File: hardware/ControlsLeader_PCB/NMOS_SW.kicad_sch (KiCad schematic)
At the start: 4 parts, among them Q15 NMOS

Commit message: DONE!!! - just need to add footprints + part #s)
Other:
- note added: "NMOS 24v -> 3.3v Signal Converter"
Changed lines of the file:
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@@
+		)
+	)
+	(text "NMOS 24v -> 3.3v Signal Converter"
+		(exclude_from_sim no)
+		(at 141.478 70.104 0)
+		(effects
+			(font
+				(size 1.905 1.905)
+				(thickness 0.254)
+				(bold yes)
+			)
 		)
 	)

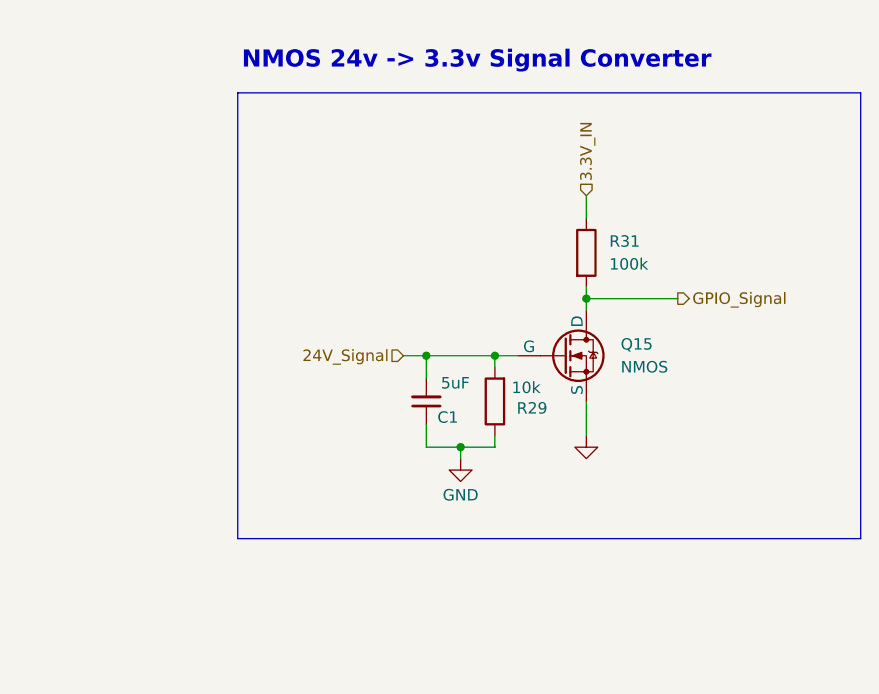
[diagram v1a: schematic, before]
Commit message: Schematic Ready for Review - Just need FET footprints to be confirmed
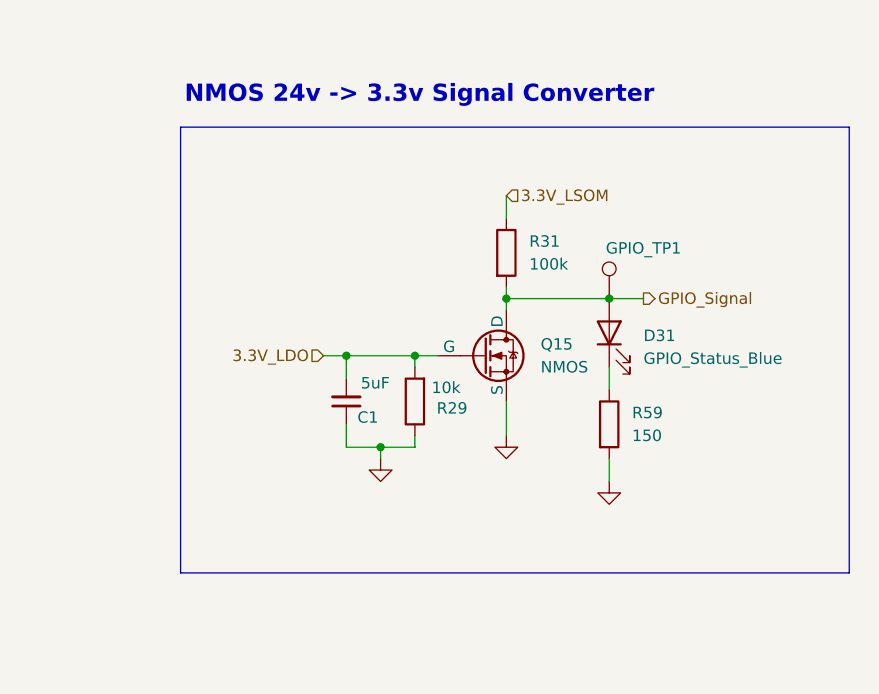
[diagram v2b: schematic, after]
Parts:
- added D31: GPIO_Status_Blue, LED_SMD:LED_0201_0603Metric_Pad0.64x0.40mm_HandSolder, symbol Device:LED
- added GPIO_TP1: TestPoint, TestPoint:TestPoint_Pad_1.0x1.0mm, symbol Connector:TestPoint
- added R59: 150, Capacitor_SMD:C_0201_0603Metric_Pad0.64x0.40mm_HandSolder, symbol Device:R
- C1: footprint Capacitor_SMD:C_0805_2012Metric -> Capacitor_SMD:C_0603_1608Metric_Pad1.08x0.95mm_HandSolder
- R29: footprint Resistor_SMD:R_0805_2012Metric -> Capacitor_SMD:C_0201_0603Metric_Pad0.64x0.40mm_HandSolder
- R31: footprint (none) -> Capacitor_SMD:C_0201_0603Metric_Pad0.64x0.40mm_HandSolder
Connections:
- net GND: now also R59.2
- net GPIO_Signal: now also D31.2 (A), GPIO_TP1.1
- net 24V_Signal renamed 3.3V_LDO
- net 3.3V_IN renamed 3.3V_LSOM
- new net: D31.1 (K), R59.1
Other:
- moved on the sheet: C1, Q15, R29, R31

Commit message: Ready for final review
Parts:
- D1: renamed from D31; Distributor Link (none) -> https://www.digikey.com/en/products/detail/ams-osram-usa-in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; Manufacturer (none) -> DigiKey; Manufacturer Prt # (none) -> LB Q99G.01-P1R1-35-1-5-R18
- Q15: footprint (none) -> LSOM_IRLM:SOT23
- renumbered R29 to R16, R31 to R17, R59 to R29, GPIO_TP1 to TP2
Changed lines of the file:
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@@
 		(dnp no)
 		(fields_autoplaced yes)
-		(property "Reference" "#PWR049"
+		(property "Reference" "#PWR036"
 			(at 156.21 123.19 0)
 			(effects
@@
 		(instances
 			(project "ControlsLeader_PCB"
-				(path "/298dad81-302c-41c7-874b-fcde1c3cde17/b17bad26-1d2e-4521-b2ad-37a0683696f4"
-					(reference "#PWR049")
-					(unit 1)
-				)
 				(path "/298dad81-302c-41c7-874b-fcde1c3cde17/cf34858a-7a31-4837-b51d-ee9ae3dd074c/879fa84f-14ed-4d21-9f88-1baa6fbdbf33"
 					(reference "#PWR087")
@@
 				(path "/298dad81-302c-41c7-874b-fcde1c3cde17/cf34858a-7a31-4837-b51d-ee9ae3dd074c/ed43737a-66c9-4099-9c79-193ec40f0132"
 					(reference "#PWR088")
+					(unit 1)
+				)
+				(path "/298dad81-302c-41c7-874b-fcde1c3cde17/cf34858a-7a31-4837-b51d-ee9ae3dd074c/f6cf8ad6-a024-4eda-a711-34d588471472"
+					(reference "#PWR036")
 					(unit 1)
 				)
@@
 		(dnp no)
 		(fields_autoplaced yes)
-		(property "Reference" "#PWR072"
+		(property "Reference" "#PWR033"
 			(at 144.78 118.11 0)
 			(effects
@@
 		(instances
 			(project "ControlsLeader_PCB"
-				(path "/298dad81-302c-41c7-874b-fcde1c3cde17/b17bad26-1d2e-4521-b2ad-37a0683696f4"
-					(reference "#PWR072")
-					(unit 1)
-				)
 				(path "/298dad81-302c-41c7-874b-fcde1c3cde17/cf34858a-7a31-4837-b51d-ee9ae3dd074c/879fa84f-14ed-4d21-9f88-1baa6fbdbf33"
 					(reference "#PWR024")
@@
 				(path "/298dad81-302c-41c7-874b-fcde1c3cde17/cf34858a-7a31-4837-b51d-ee9ae3dd074c/ed43737a-66c9-4099-9c79-193ec40f0132"
 					(reference "#PWR025")
+					(unit 1)
+				)
+				(path "/298dad81-302c-41c7-874b-fcde1c3cde17/cf34858a-7a31-4837-b51d-ee9ae3dd074c/f6cf8ad6-a024-4eda-a711-34d588471472"
+					(reference "#PWR033")
 					(unit 1)
 				)
@@
 		(instances
 			(project "ControlsLeader_PCB"
-				(path "/298dad81-302c-41c7-874b-fcde1c3cde17/b17bad26-1d2e-4521-b2ad-37a0683696f4"
-					(reference "C1")
-					(unit 1)
-				)
 				(path "/298dad81-302c-41c7-874b-fcde1c3cde17/cf34858a-7a31-4837-b51d-ee9ae3dd074c/879fa84f-14ed-4d21-9f88-1baa6fbdbf33"
 					(reference "C2")
@@
 				(path "/298dad81-302c-41c7-874b-fcde1c3cde17/cf34858a-7a31-4837-b51d-ee9ae3dd074c/ed43737a-66c9-4099-9c79-193ec40f0132"
 					(reference "C14")
+					(unit 1)
+				)
+				(path "/298dad81-302c-41c7-874b-fcde1c3cde17/cf34858a-7a31-4837-b51d-ee9ae3dd074c/f6cf8ad6-a024-4eda-a711-34d588471472"
+					(reference "C1")
 					(unit 1)
 				)
@@
 		(dnp no)
 		(fields_autoplaced yes)
-		(property "Reference" "R59"
+		(property "Reference" "R29"
 			(at 158.75 109.2199 0)
 			(effects
@@
 		(instances
 			(project "ControlsLeader_PCB"
-				(path "/298dad81-302c-41c7-874b-fcde1c3cde17/b17bad26-1d2e-4521-b2ad-37a0683696f4"
-					(reference "R59")
-					(unit 1)
-				)
 				(path "/298dad81-302c-41c7-874b-fcde1c3cde17/cf34858a-7a31-4837-b51d-ee9ae3dd074c/879fa84f-14ed-4d21-9f88-1baa6fbdbf33"
 					(reference "R71")
@@
 				(path "/298dad81-302c-41c7-874b-fcde1c3cde17/cf34858a-7a31-4837-b51d-ee9ae3dd074c/ed43737a-66c9-4099-9c79-193ec40f0132"
 					(reference "R72")
+					(unit 1)
+				)
+				(path "/298dad81-302c-41c7-874b-fcde1c3cde17/cf34858a-7a31-4837-b51d-ee9ae3dd074c/f6cf8ad6-a024-4eda-a711-34d588471472"
+					(reference "R29")
 					(unit 1)
 				)
@@
 			)
 		)
-		(property "Footprint" ""
+		(property "Footprint" "LSOM_IRLM:SOT23"
 			(at 147.32 100.33 0)
 			(effects
@@
 		(instances
 			(project "ControlsLeader_PCB"
-				(path "/298dad81-302c-41c7-874b-fcde1c3cde17/b17bad26-1d2e-4521-b2ad-37a0683696f4"
-					(reference "Q15")
-					(unit 1)
-				)
 				(path "/298dad81-302c-41c7-874b-fcde1c3cde17/cf34858a-7a31-4837-b51d-ee9ae3dd074c/879fa84f-14ed-4d21-9f88-1baa6fbdbf33"
 					(reference "Q5")
@@
 				(path "/298dad81-302c-41c7-874b-fcde1c3cde17/cf34858a-7a31-4837-b51d-ee9ae3dd074c/ed43737a-66c9-4099-9c79-193ec40f0132"
 					(reference "Q2")
+					(unit 1)
+				)
+				(path "/298dad81-302c-41c7-874b-fcde1c3cde17/cf34858a-7a31-4837-b51d-ee9ae3dd074c/f6cf8ad6-a024-4eda-a711-34d588471472"
+					(reference "Q15")
 					(unit 1)
 				)
@@
 		(dnp no)
 		(fields_autoplaced yes)
-		(property "Reference" "D31"
+		(property "Reference" "D1"
 			(at 160.02 100.6474 90)
 			(effects
@@
 			)
 		)
-		(property "Distributor Link" ""
+		(property "Distributor Link" "https://www.digikey.com/en/products/detail/ams-osram-usa-inc/LB-Q99G-01-P1R1-35-1-5-R18/21556500"
 			(at 156.21 100.33 90)
 			(effects
@@
 			)
 		)
-		(property "Manufacturer" ""
+		(property "Manufacturer" "DigiKey"
 			(at 156.21 100.33 90)
 			(effects
@@
 			)
 		)
-		(property "Manufacturer Prt #" ""
+		(property "Manufacturer Prt #" "LB Q99G.01-P1R1-35-1-5-R18"
 			(at 156.21 100.33 90)
 			(effects
@@
 		(instances
 			(project "ControlsLeader_PCB"
-				(path "/298dad81-302c-41c7-874b-fcde1c3cde17/b17bad26-1d2e-4521-b2ad-37a0683696f4"
-					(reference "D31")
-					(unit 1)
-				)
 				(path "/298dad81-302c-41c7-874b-fcde1c3cde17/cf34858a-7a31-4837-b51d-ee9ae3dd074c/879fa84f-14ed-4d21-9f88-1baa6fbdbf33"
 					(reference "D43")
@@
 				(path "/298dad81-302c-41c7-874b-fcde1c3cde17/cf34858a-7a31-4837-b51d-ee9ae3dd074c/ed43737a-66c9-4099-9c79-193ec40f0132"
 					(reference "D44")
+					(unit 1)
+				)
+				(path "/298dad81-302c-41c7-874b-fcde1c3cde17/cf34858a-7a31-4837-b51d-ee9ae3dd074c/f6cf8ad6-a024-4eda-a711-34d588471472"
+					(reference "D1")
 					(unit 1)
 				)
@@
 		(dnp no)
 		(fields_autoplaced yes)
-		(property "Reference" "R31"
+		(property "Reference" "R17"
 			(at 147.32 90.1699 0)
 			(effects
@@
 		(instances
 			(project "ControlsLeader_PCB"
-				(path "/298dad81-302c-41c7-874b-fcde1c3cde17/b17bad26-1d2e-4521-b2ad-37a0683696f4"
-					(reference "R31")
-					(unit 1)
-				)
 				(path "/298dad81-302c-41c7-874b-fcde1c3cde17/cf34858a-7a31-4837-b51d-ee9ae3dd074c/879fa84f-14ed-4d21-9f88-1baa6fbdbf33"
 					(reference "R19")
@@
 				(path "/298dad81-302c-41c7-874b-fcde1c3cde17/cf34858a-7a31-4837-b51d-ee9ae3dd074c/ed43737a-66c9-4099-9c79-193ec40f0132"
 					(reference "R10")
+					(unit 1)
+				)
+				(path "/298dad81-302c-41c7-874b-fcde1c3cde17/cf34858a-7a31-4837-b51d-ee9ae3dd074c/f6cf8ad6-a024-4eda-a711-34d588471472"
+					(reference "R17")
 					(unit 1)
 				)
@@
 		(on_board yes)
 		(dnp no)
-		(property "Reference" "#PWR070"
+		(property "Reference" "#PWR031"
 			(at 130.81 120.65 0)
 			(effects
@@
 		(instances
 			(project "ControlsLeader_PCB"
-				(path "/298dad81-302c-41c7-874b-fcde1c3cde17/b17bad26-1d2e-4521-b2ad-37a0683696f4"
-					(reference "#PWR070")
-					(unit 1)
-				)
 				(path "/298dad81-302c-41c7-874b-fcde1c3cde17/cf34858a-7a31-4837-b51d-ee9ae3dd074c/879fa84f-14ed-4d21-9f88-1baa6fbdbf33"
 					(reference "#PWR023")
@@
 				(path "/298dad81-302c-41c7-874b-fcde1c3cde17/cf34858a-7a31-4837-b51d-ee9ae3dd074c/ed43737a-66c9-4099-9c79-193ec40f0132"
 					(reference "#PWR012")
+					(unit 1)
+				)
+				(path "/298dad81-302c-41c7-874b-fcde1c3cde17/cf34858a-7a31-4837-b51d-ee9ae3dd074c/f6cf8ad6-a024-4eda-a711-34d588471472"
+					(reference "#PWR031")
 					(unit 1)
 				)
@@
 		(on_board yes)
 		(dnp no)
-		(property "Reference" "R29"
+		(property "Reference" "R16"
 			(at 140.462 108.712 0)
 			(effects
@@
 		(instances
 			(project "ControlsLeader_PCB"
-				(path "/298dad81-302c-41c7-874b-fcde1c3cde17/b17bad26-1d2e-4521-b2ad-37a0683696f4"
-					(reference "R29")
-					(unit 1)
-				)
 				(path "/298dad81-302c-41c7-874b-fcde1c3cde17/cf34858a-7a31-4837-b51d-ee9ae3dd074c/879fa84f-14ed-4d21-9f88-1baa6fbdbf33"
 					(reference "R18")
@@
 				(path "/298dad81-302c-41c7-874b-fcde1c3cde17/cf34858a-7a31-4837-b51d-ee9ae3dd074c/ed43737a-66c9-4099-9c79-193ec40f0132"
 					(reference "R9")
+					(unit 1)
+				)
+				(path "/298dad81-302c-41c7-874b-fcde1c3cde17/cf34858a-7a31-4837-b51d-ee9ae3dd074c/f6cf8ad6-a024-4eda-a711-34d588471472"
+					(reference "R16")
 					(unit 1)
 				)
@@
 		(on_board yes)
 		(dnp no)
-		(property "Reference" "GPIO_TP1"
+		(property "Reference" "TP2"
 			(at 160.02 90.932 0)
 			(effects
@@
 		(instances
 			(project "ControlsLeader_PCB"
-				(path "/298dad81-302c-41c7-874b-fcde1c3cde17/b17bad26-1d2e-4521-b2ad-37a0683696f4"
-					(reference "GPIO_TP1")
-					(unit 1)
-				)
 				(path "/298dad81-302c-41c7-874b-fcde1c3cde17/cf34858a-7a31-4837-b51d-ee9ae3dd074c/879fa84f-14ed-4d21-9f88-1baa6fbdbf33"
 					(reference "TP14")
@@
 					(unit 1)
 				)
+				(path "/298dad81-302c-41c7-874b-fcde1c3cde17/cf34858a-7a31-4837-b51d-ee9ae3dd074c/f6cf8ad6-a024-4eda-a711-34d588471472"
+					(reference "TP2")
+					(unit 1)
+				)

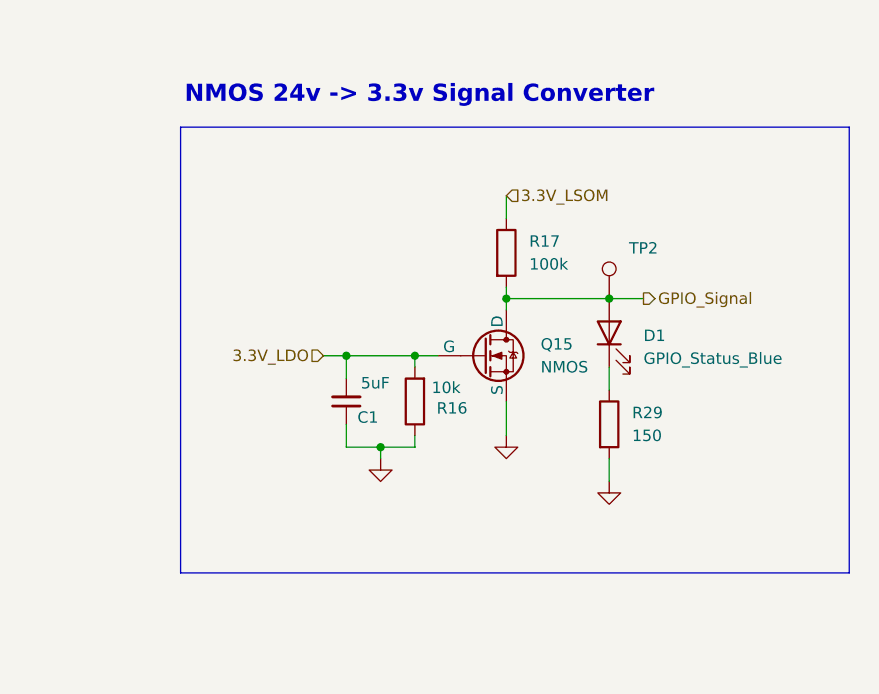
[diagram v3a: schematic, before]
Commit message: Updated LSOM status LED and horn 24v signal connector layout
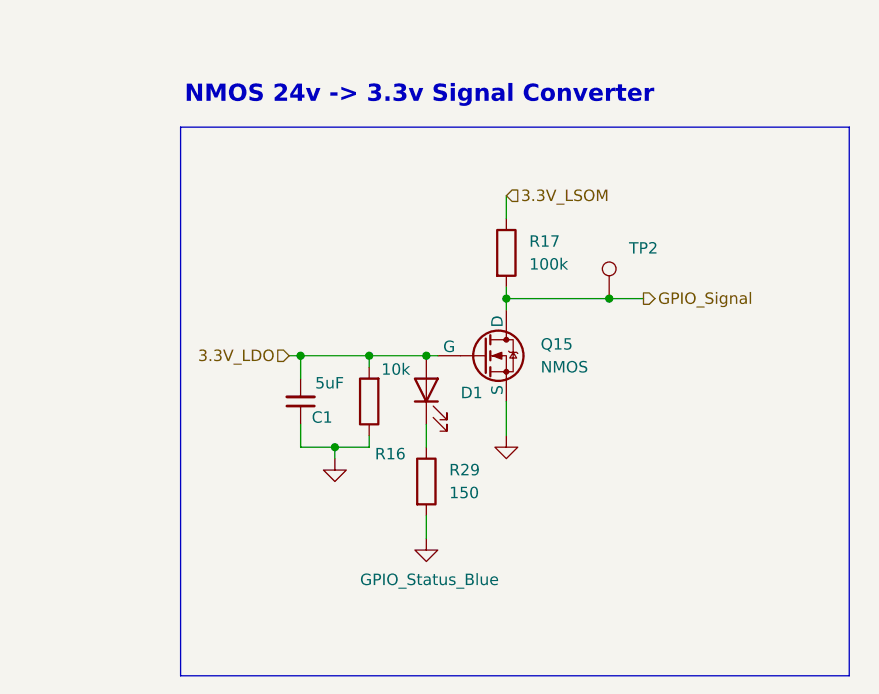
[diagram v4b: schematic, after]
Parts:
- D1: footprint LED_SMD:LED_0201_0603Metric_Pad0.64x0.40mm_HandSolder -> LED_SMD:LED_0603_1608Metric_Pad1.05x0.95mm_HandSolder
- R16, R17, R29: footprint Capacitor_SMD:C_0201_0603Metric_Pad0.64x0.40mm_HandSolder -> Capacitor_SMD:C_0603_1608Metric_Pad1.08x0.95mm_HandSolder
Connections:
- net 3.3V_LDO: now also D1.2 (A)
- net GPIO_Signal: no longer D1.2 (A)
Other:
- moved on the sheet: C1, D1, R16, R29

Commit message: Schematic RevA
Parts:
- removed Q15: NMOS, LSOM_IRLM:SOT23, symbol Simulation_SPICE:NMOS
- removed R16: 10k, Capacitor_SMD:C_0603_1608Metric_Pad1.08x0.95mm_HandSolder, symbol Device:R
- removed R17: 100k, Capacitor_SMD:C_0603_1608Metric_Pad1.08x0.95mm_HandSolder, symbol Device:R
- removed R29: 150, Capacitor_SMD:C_0603_1608Metric_Pad1.08x0.95mm_HandSolder, symbol Device:R
- removed TP2: TestPoint, TestPoint:TestPoint_Pad_1.0x1.0mm, symbol Connector:TestPoint
- added Q1: NMOS, LSOM_IRLM:SOT23, symbol Simulation_SPICE:NMOS
- added R1: 10k, Capacitor_SMD:C_0603_1608Metric_Pad1.08x0.95mm_HandSolder, symbol Device:R
- added R31: 100k, Capacitor_SMD:C_0603_1608Metric_Pad1.08x0.95mm_HandSolder, symbol Device:R
- added R9: 150, Capacitor_SMD:C_0603_1608Metric_Pad1.08x0.95mm_HandSolder, symbol Device:R
- added TP1: TestPoint, TestPoint:TestPoint_Pad_1.0x1.0mm, symbol Connector:TestPoint
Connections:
- net 3.3V_LSOM: now also R31.1
- net GND: now also Q1.3 (S), R1.1, R9.2
- net GPIO_Signal: now also Q1.1 (D), R31.2, TP1.1
- net at D1.1 (K): now also R9.1
- net 3.3V_LDO renamed 3.3V_LDO_Switch
- net 3.3V_LDO_Switch: now also Q1.2 (G), R1.2

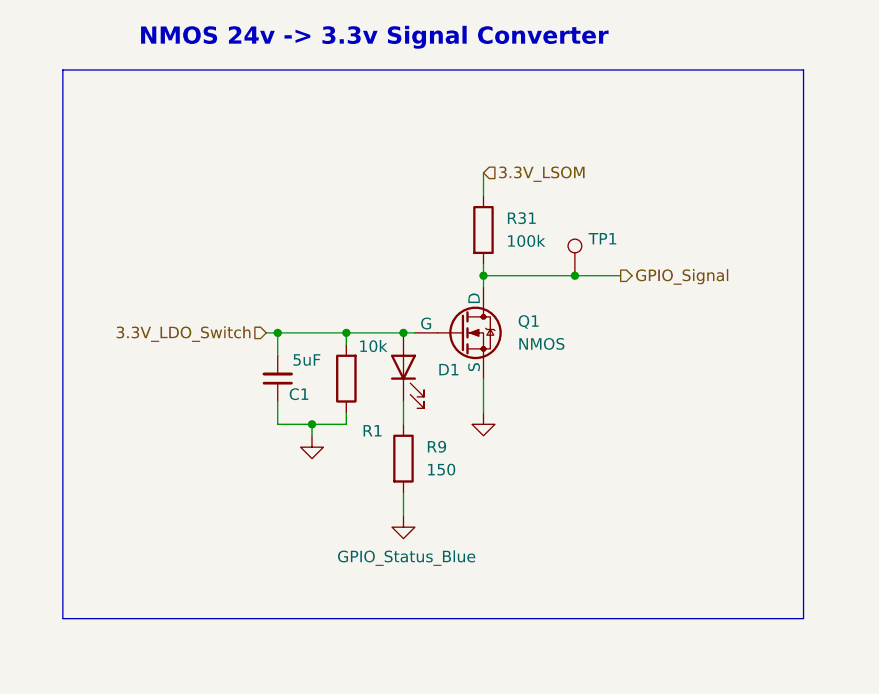
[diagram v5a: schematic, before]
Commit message: PCB DESIGN DONE - need to add datasheets and p/n
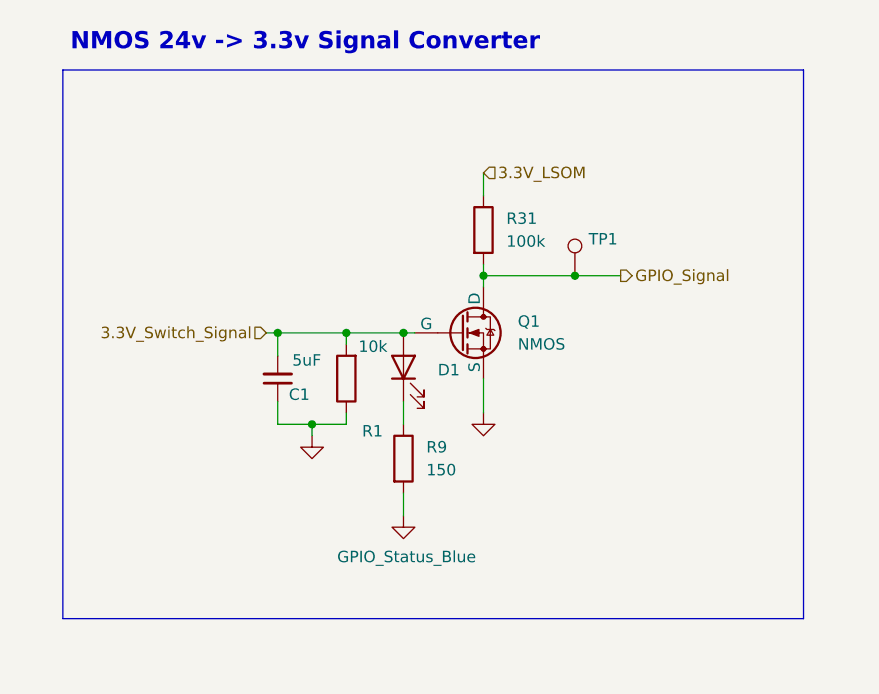
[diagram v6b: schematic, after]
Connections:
- net 3.3V_LDO_Switch renamed 3.3V_Switch_Signal
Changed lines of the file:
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@@
 	(text "NMOS 24v -> 3.3v Signal Converter"
 		(exclude_from_sim no)
-		(at 130.048 67.564 0)
+		(at 122.428 68.072 0)
 		(effects
 			(font
@@
 		)
 	)
-	(hierarchical_label "3.3V_LDO_Switch"
+	(hierarchical_label "3.3V_Switch_Signal"
 		(shape input)
 		(at 118.11 100.33 180)

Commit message: BOM!
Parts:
- D1: P/N (none) -> LB Q99G.01-P1R1-35-1-5-R18
- Q1: P/N (none) -> IRLML2030TRPBF
- R1: footprint Capacitor_SMD:C_0603_1608Metric_Pad1.08x0.95mm_HandSolder -> Resistor_SMD:R_0603_1608Metric_Pad0.98x0.95mm_HandSolder; P/N CRCW080510K0FKEAC -> CRCW060310K0FKTAHP
- R31: footprint Capacitor_SMD:C_0603_1608Metric_Pad1.08x0.95mm_HandSolder -> Resistor_SMD:R_0603_1608Metric_Pad0.98x0.95mm_HandSolder; P/N (none) -> CRCW0603100KFKTAHP
- R9: footprint Capacitor_SMD:C_0603_1608Metric_Pad1.08x0.95mm_HandSolder -> Resistor_SMD:R_0603_1608Metric_Pad0.98x0.95mm_HandSolder; P/N (none) -> ERJ-P03F1500V
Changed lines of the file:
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@@
 			)
 		)
-		(property "Description" "Unpolarized capacitor, small symbol"
+		(property "Description" "NMOS cap c13"
 			(at 119.38 105.41 0)
 			(effects
@@
 			)
 		)
-		(property "Footprint" "Capacitor_SMD:C_0603_1608Metric_Pad1.08x0.95mm_HandSolder"
+		(property "Footprint" "Resistor_SMD:R_0603_1608Metric_Pad0.98x0.95mm_HandSolder"
 			(at 131.572 114.3 90)
 			(effects
@@
 			)
 		)
-		(property "Description" "Resistor"
+		(property "Description" "NMOS 150Ohms"
 			(at 133.35 114.3 0)
 			(effects
@@
 		)
 		(property "Manufacturer Prt #" ""
+			(at 133.35 114.3 0)
+			(effects
+				(font
+					(size 1.27 1.27)
+				)
+				(hide yes)
+			)
+		)
+		(property "P/N" "ERJ-P03F1500V"
 			(at 133.35 114.3 0)
 			(effects
@@
 			)
 		)
-		(property "Description" "N-MOSFET transistor, drain/source/gate"
+		(property "Description" "NMOS!"
 			(at 139.7 100.33 0)
 			(effects
@@
 		)
 		(property "Manufacturer Prt #" ""
+			(at 139.7 100.33 0)
+			(effects
+				(font
+					(size 1.27 1.27)
+				)
+				(hide yes)
+			)
+		)
+		(property "P/N" "IRLML2030TRPBF"
 			(at 139.7 100.33 0)
 			(effects
@@
 			)
 		)
-		(property "Footprint" "Capacitor_SMD:C_0603_1608Metric_Pad1.08x0.95mm_HandSolder"
+		(property "Footprint" "Resistor_SMD:R_0603_1608Metric_Pad0.98x0.95mm_HandSolder"
 			(at 128.778 105.41 90)
 			(effects
@@
 			)
 		)
-		(property "Description" "Resistor"
+		(property "Description" "NOMS 10k"
 			(at 127 105.41 0)
 			(effects
@@
 			)
 		)
-		(property "P/N" "CRCW080510K0FKEAC"
+		(property "P/N" "CRCW060310K0FKTAHP"
 			(at 127 105.41 0)
 			(effects
@@
 			)
 		)
-		(property "Description" "test point"
+		(property "Description" ""
+			(at 152.4 93.98 0)
+			(effects
+				(font
+					(size 1.27 1.27)
+				)
+				(hide yes)
+			)
+		)
+		(property "P/N" "~"
 			(at 152.4 93.98 0)
 			(effects
@@
 			)
 		)
-		(property "Description" "Light emitting diode"
+		(property "Description" "NMOS LEDs"
 			(at 133.35 104.14 0)
 			(effects
@@
 		)
 		(property "Manufacturer Prt #" "LB Q99G.01-P1R1-35-1-5-R18"
+			(at 133.35 104.14 90)
+			(effects
+				(font
+					(size 1.27 1.27)
+				)
+				(hide yes)
+			)
+		)
+		(property "P/N" "LB Q99G.01-P1R1-35-1-5-R18"
 			(at 133.35 104.14 90)
 			(effects
@@
 			)
 		)
-		(property "Footprint" "Capacitor_SMD:C_0603_1608Metric_Pad1.08x0.95mm_HandSolder"
+		(property "Footprint" "Resistor_SMD:R_0603_1608Metric_Pad0.98x0.95mm_HandSolder"
 			(at 140.462 88.9 90)
 			(effects
@@
 			)
 		)
-		(property "Description" "Resistor"
+		(property "Description" "NMOS 100k"
 			(at 142.24 88.9 0)
 			(effects
@@
 			(at 142.24 88.9 0)
 			(effects
+				(font
+					(size 1.27 1.27)
+				)
+				(hide yes)
+			)
+		)
+		(property "P/N" "CRCW0603100KFKTAHP"
+			(at 142.24 88.9 0)
+			(effects
